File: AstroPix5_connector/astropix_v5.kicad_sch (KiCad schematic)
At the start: 46 parts, among them J1 HBOut, J10 SPI_right, J12 Measures_Analog, J14 Bias, J2 Conn_01x05, J3 pcie_GECCO, J4 HBOut, J5 HBOut, J7 HV_in_external, J8 Conn_01x03, J9 SPI_left, U2 AstroPix5_split_powerring

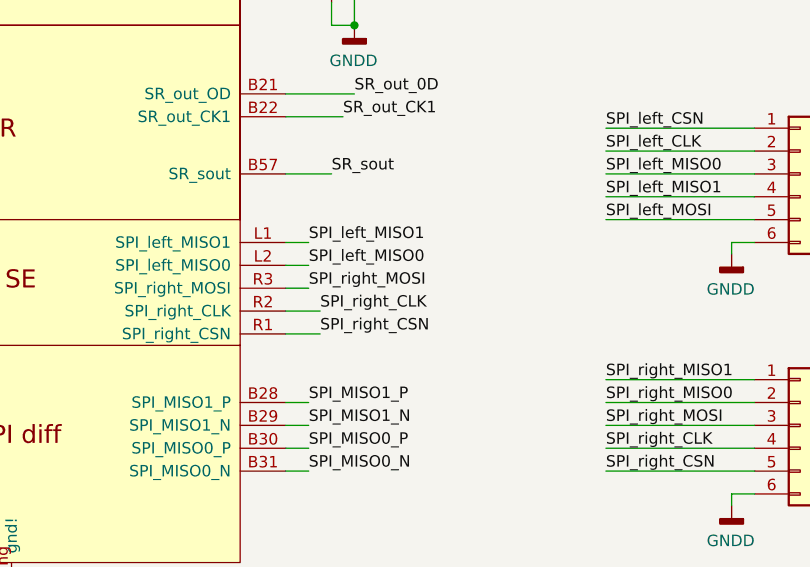
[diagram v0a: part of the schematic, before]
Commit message: Added series resistors to SPI lines
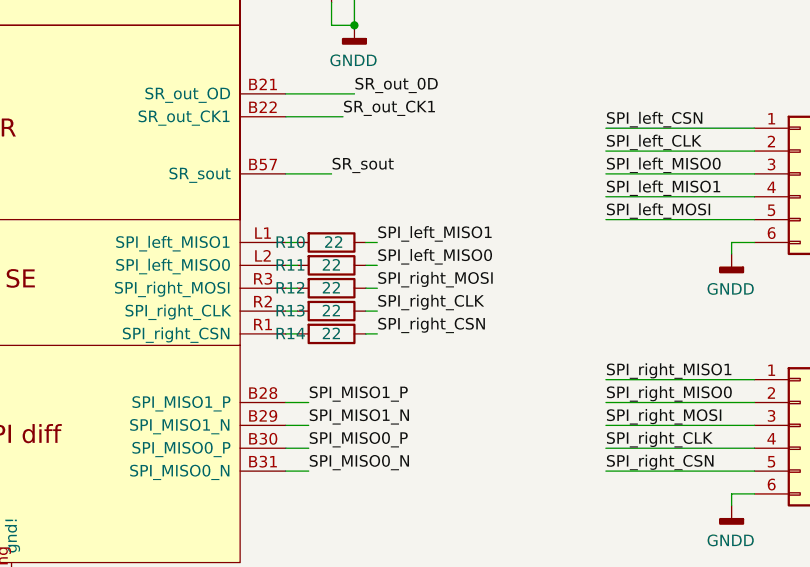
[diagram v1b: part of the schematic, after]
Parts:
- added R10, R11, R12, R13, R14: 22, Resistor_SMD:R_0402_1005Metric, symbol Device:R
- C12, C16, C17, C18: KiLib_Generator (none) -> SMD_2terminal_chip_molded
- J10, J9: KiLib_Generator (none) -> connector/pin_header_socket
- J3: footprint Connector_PCBEdge:BUS_PCIexpress_x16 -> Connector_PCBEdge:BUS_PCIexpress_x16_ilo
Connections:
- net SPI_left_MISO0: now also R11.1; no longer U2.L2 (SPI_left_MISO0)
- net SPI_left_MISO1: now also R10.1; no longer U2.L1 (SPI_left_MISO1)
- net SPI_right_CLK: now also R13.1; no longer U2.R2 (SPI_right_CLK)
- net SPI_right_CSN: now also R14.1; no longer U2.R1 (SPI_right_CSN)
- net SPI_right_MOSI: now also R12.1; no longer U2.R3 (SPI_right_MOSI)
- new net: R11.2, U2.L2 (SPI_left_MISO0)
- new net: R10.2, U2.L1 (SPI_left_MISO1)
- new net: R14.2, U2.R1 (SPI_right_CSN)
- new net: R13.2, U2.R2 (SPI_right_CLK)
- new net: R12.2, U2.R3 (SPI_right_MOSI)

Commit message: Improve schematic readability and fix overlapping labels
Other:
- note removed: "ni"
- moved on the sheet: C1, C10, C11, C12, C13, C14, C15, C16, C17, C18, C2, C3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

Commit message: Fix duplicate SR_load in schematic + layout and adjust DigInj text in schematic
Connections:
- net SR_load: no longer J3.B54 (FMC_LA02_P)
- no-connect marks 54 -> 55
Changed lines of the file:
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@@
 	(text "If injection card is not used"
 		(exclude_from_sim no)
-		(at 166.37 269.24 0)
+		(at 165.354 264.16 0)
 		(effects
 			(font
@@
 	)
 	(no_connect
+		(at 148.59 271.78)
+	)
+	(no_connect
 		(at 104.14 139.7)
 	)
@@
 	(wire
 		(pts
-			(xy 148.59 271.78) (xy 156.21 271.78)
-		)
-		(stroke
-			(width 0)
-			(type default)
-		)
-	)
-	(wire
-		(pts
 			(xy 354.33 160.02) (xy 354.33 158.75)
 		)
@@
 		(effects
 			(font
-				(size 1.27 1.27)
-			)
-			(justify left bottom)
-		)
-	)
-	(label "SR_load"
-		(at 156.21 271.78 0)
-		(effects
-			(font
